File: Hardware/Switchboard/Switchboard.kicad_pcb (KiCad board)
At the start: 2 copper layers, 99.1 x 48.3 mm, 50 parts, among them J1 S88_In_Header, J2 S88_In_Plug, J3 S88_Out_Header, J4 S88_Out_Plug, Q1 BC237, SW1 SW_Push, SW2 SW_Push, SW3 SW_Push, SW4 SW_Push, SW5 SW_Push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

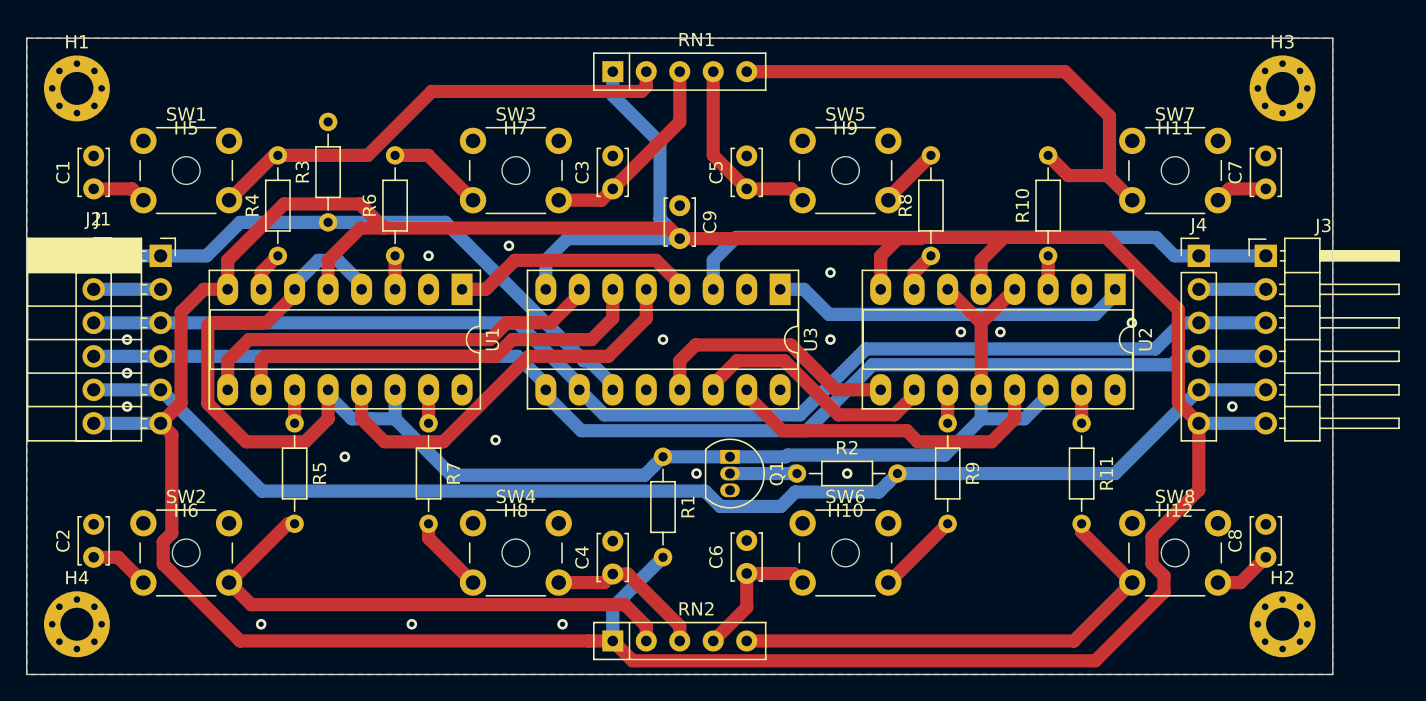
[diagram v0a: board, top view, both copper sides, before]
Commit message: Converted mounting holes to vias
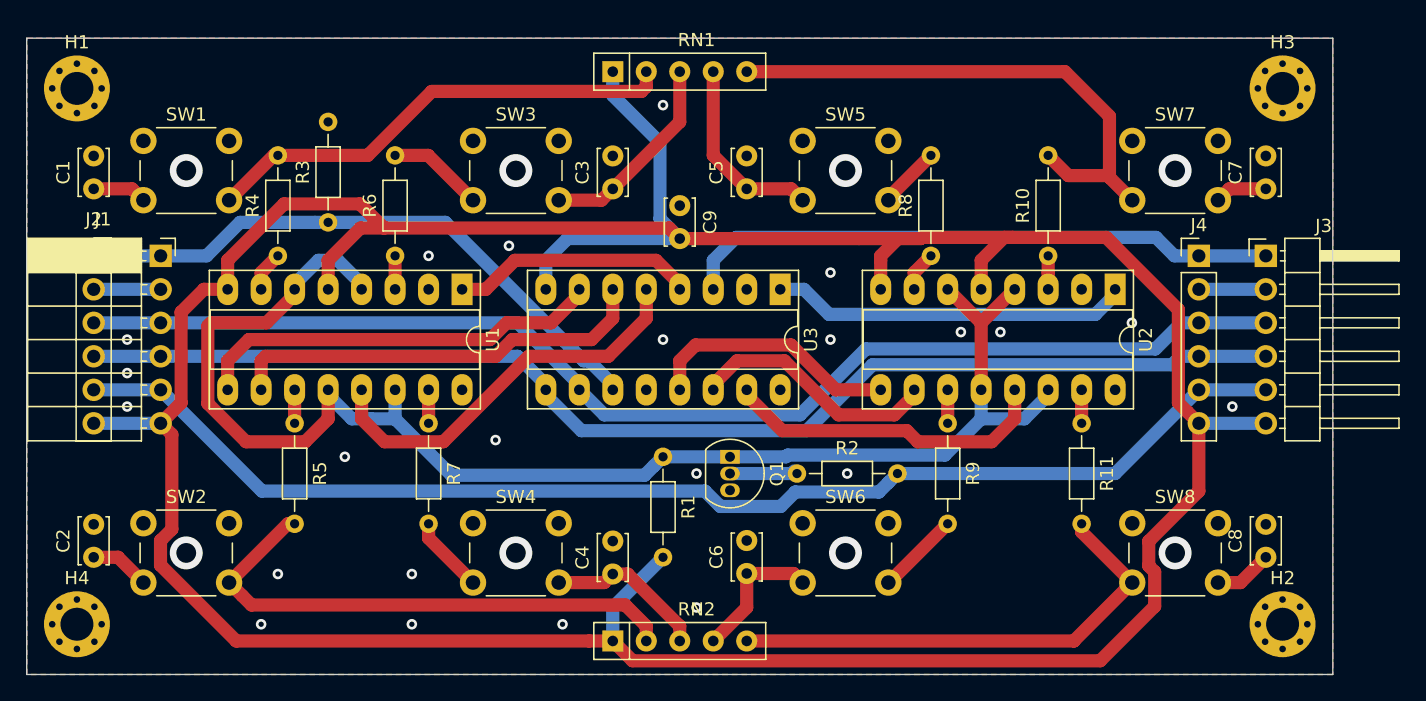
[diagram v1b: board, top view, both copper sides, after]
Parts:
- removed H10, H11, H12, H5, H6, H7, H8, H9: MountingHole, MountingHole:MountingHole_2.1mm
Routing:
- net GND: vias 19 -> 23
- net (no net): vias 0 -> 8
